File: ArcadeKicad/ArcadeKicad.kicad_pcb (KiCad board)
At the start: 2 copper layers, 60 x 60 mm, 25 parts, among them J2 TVout, J3 joystick, J4 Bornera, SW1 SW_Push, U1 ATMEGA328P-PU, U2 L7805, Y1 Crystal_Small

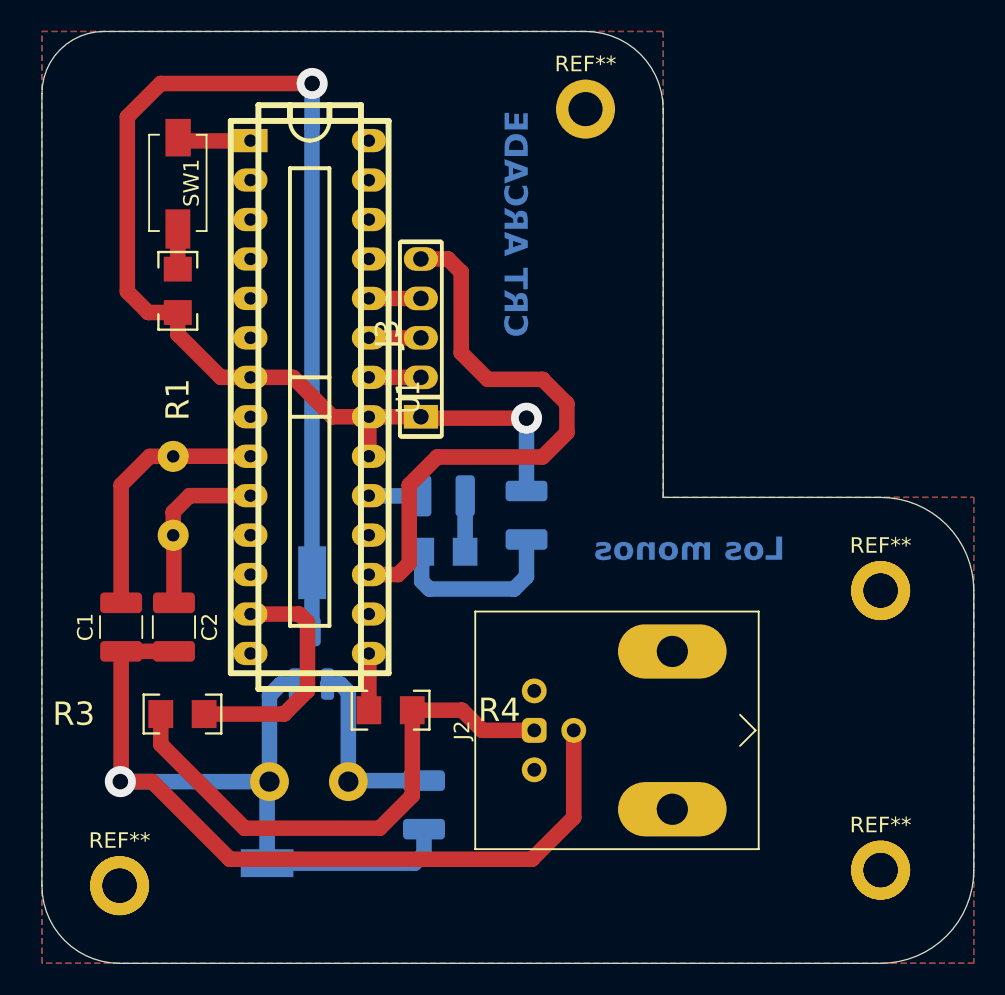
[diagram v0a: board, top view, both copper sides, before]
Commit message: cambios pcb
agregue los nombres de los integrantes y el simbolo de la paz
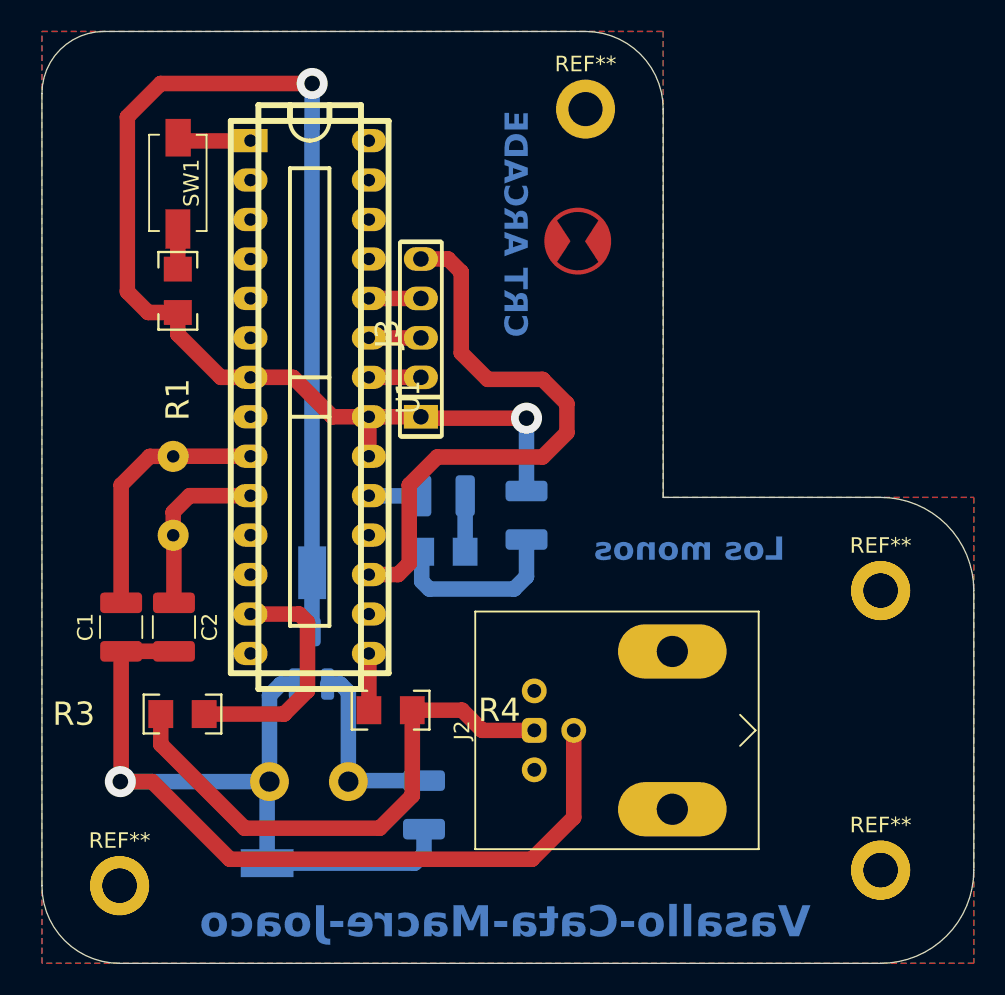
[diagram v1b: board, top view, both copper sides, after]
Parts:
- added G***: LOGO, footprint:simbolo_paz, F.Cu at (74.5, 53.5)
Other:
- board text added: "Vasallo-Cata-Macre-Joaco"
